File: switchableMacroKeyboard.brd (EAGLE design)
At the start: 58.4 x 110.5 mm, 33 parts

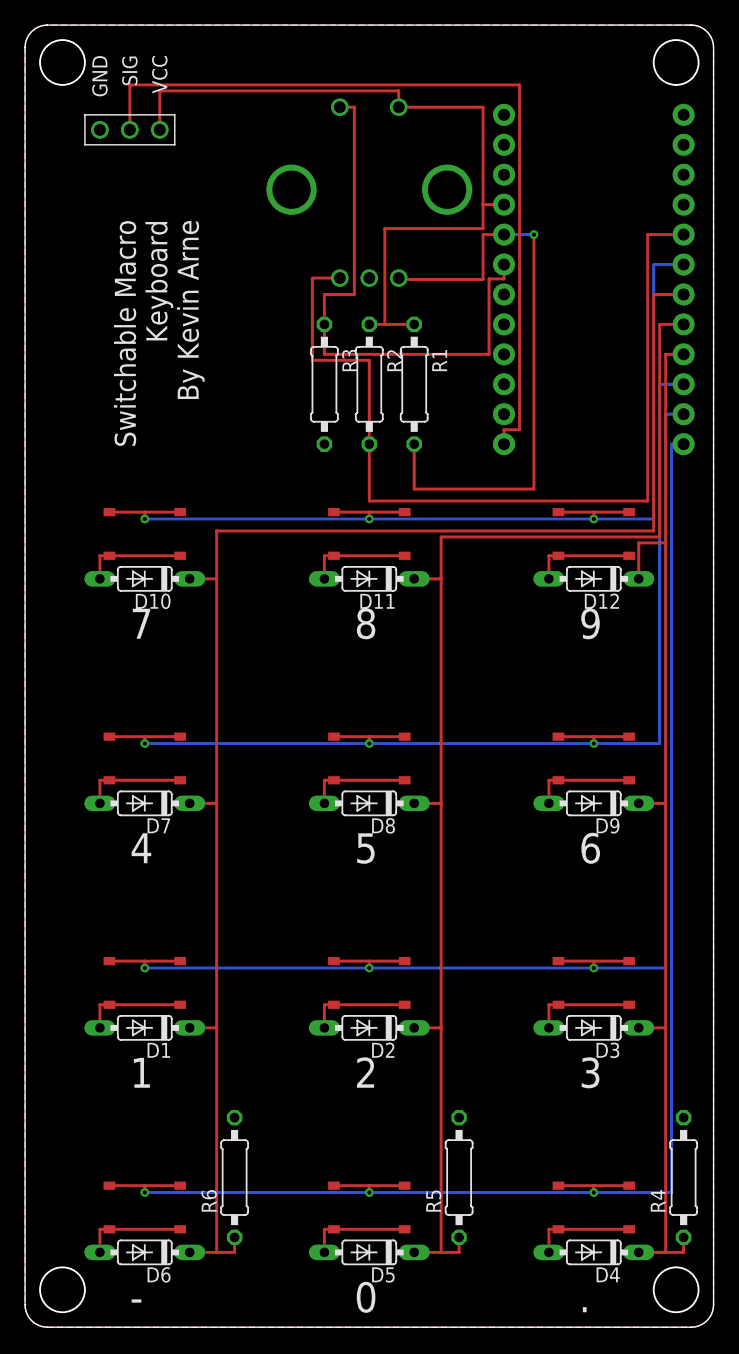
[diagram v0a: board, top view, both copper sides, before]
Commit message: Added an enable option to disable all output when broken for debugging purposes. Mitered all of the traces with a 40 mil miter. Changed the corners from filets to chamfers.
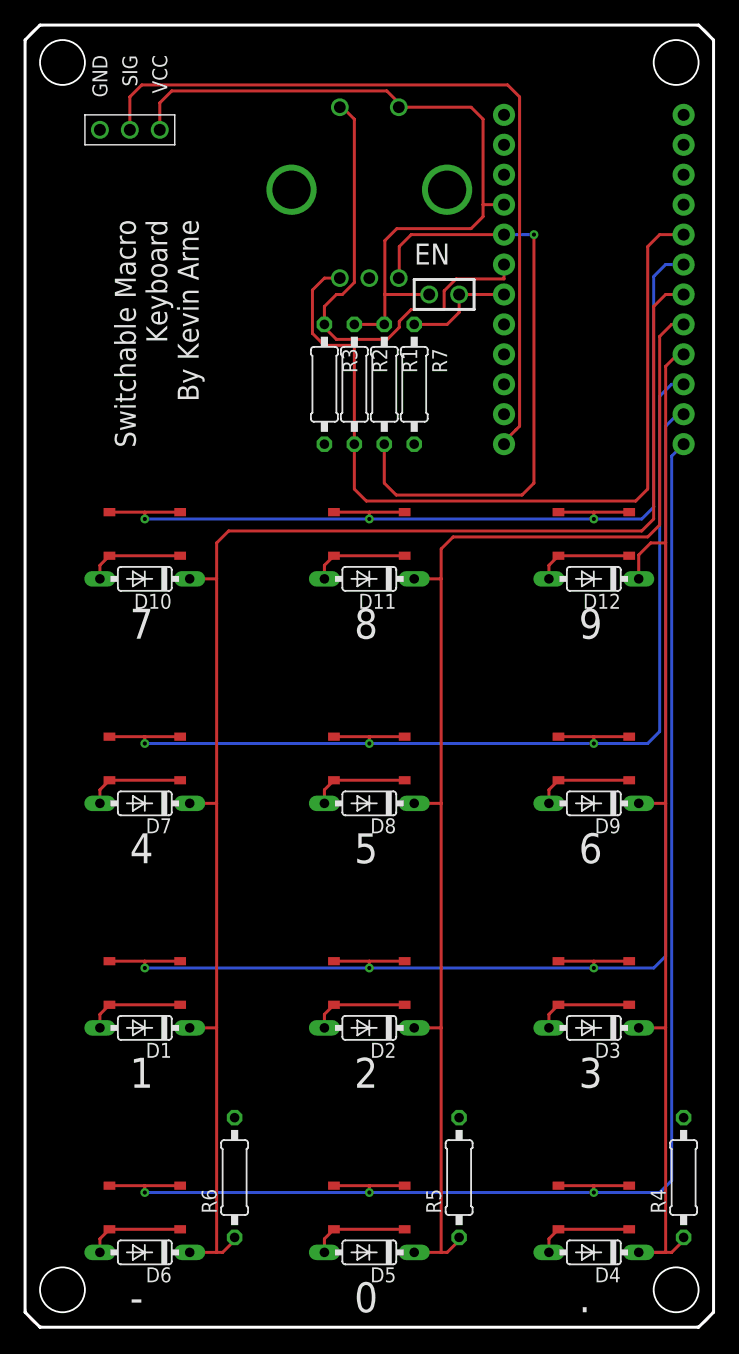
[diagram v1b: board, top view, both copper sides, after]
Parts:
- added R7: 10k, rcl:0207/10
- added U$1, U$2: TESTPOINT, ARNEConnectors:TESTPOINT
- moved R1 2.54 mm to (30.5, 80.0)
- moved R2 1.27 mm to (27.9, 80.0)
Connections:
- new net EN: B1.18, R7.1, U$2.1
- net GND: now also R7.2
- net VCC: now also U$1.1
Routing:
- net EN: track 0.00 -> 9.56 mm
- net SW-SIG: track 47.6 -> 40.9 mm
- net N$12: track 75.3 -> 72.4 mm
- net N$28: track 132.8 -> 130.5 mm
- net N$22: track 111.3 -> 108.9 mm
- net LCDSIG: track 68.7 -> 66.7 mm
- net N$30: track 95.0 -> 93.2 mm
- net N$9: track 51.0 -> 52.5 mm
- net N$24: track 87.0 -> 85.9 mm
- net N$2: track 129.0 -> 127.8 mm
- net N$17: track 95.9 -> 94.7 mm
- net N$10: track 112.4 -> 111.3 mm
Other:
- outline, holes or cut-outs redrawn
- board text added: "EN"
